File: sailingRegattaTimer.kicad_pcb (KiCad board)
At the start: 2 copper layers, 25 parts, among them J1-Red-1M1 Conn_01x02_Socket, J10-12v-In1 Conn_01x02_Socket, J2-Yel-2M1 Conn_01x02_Socket, J3-Grn-3M1 J3-Grn-3M, J4-Blu-5M1 J4-Blu-5M1, J5-5v-LED1 Conn_01x02_Socket, J6-Reset1 J6-Reset, J7-Ext-Buz1 Conn_01x02_Socket, J8-Pololu-VReg1 Conn_01x04_Socket, J9-Relay1 Conn_01x03_Socket

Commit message: incremental save updated schematic and pcb
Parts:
- moved R5 60.7 mm to (160.1, 64.0)
- moved J8-Pololu-VReg1 49.2 mm to (168.0, 48.7)
- moved J10-12v-In1 46.1 mm to (176.0, 51.8)
- moved J9-Relay1 37.3 mm to (171.0, 78.9)
- moved J3-Grn-3M1 32.9 mm to (210.5, 71.8)
- moved J4-Blu-5M1 32.8 mm to (210.5, 80.8)
- moved R2 32.1 mm to (202.5, 64.6)
- moved J2-Yel-2M1 32.0 mm to (210.5, 62.2)
- moved J1-Red-1M1 31.6 mm to (210.5, 52.8)
- moved R1 31.5 mm to (202.5, 55.3)
- moved R4 31.5 mm to (202.5, 83.3)
- moved R3 31.5 mm to (202.5, 74.0)
- moved SW4-Blu-5M1 30.2 mm to (191.5, 79.3)
- moved SW3-Grn-3M1 30.0 mm to (191.5, 70.0)
- moved J5-5v-LED1 29.9 mm to (163.5, 82.0)
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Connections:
- A1 pad 29: unconnected-(A1-GND-Pad29) -> GND
- A1 pad 5: unconnected-(A1-+5V-Pad5) -> +5V
- A1 pad 6: unconnected-(A1-GND-Pad6) -> GND
- A1 pad 7: unconnected-(A1-GND-Pad7) -> GND
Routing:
- net GND: track 0.00 -> 180.1 mm
- net +5V: track 0.00 -> 110.7 mm
- net Net-(A1-D4): track 0.00 -> 70.5 mm
- net Net-(A1-~{RESET}): track 0.00 -> 67.9 mm
- net Net-(A1-D2): track 0.00 -> 55.0 mm
- net Net-(A1-D7): track 0.00 -> 45.1 mm, vias 0 -> 1
- net Net-(A1-D8): track 0.00 -> 35.7 mm, vias 0 -> 1
- net Net-(A1-VIN): track 0.00 -> 34.8 mm
- net Net-(A1-D12): track 0.00 -> 29.0 mm
- net Net-(A1-D3): track 0.00 -> 27.3 mm
- net Net-(A1-D5): track 0.00 -> 22.9 mm
- net Net-(D1-LED1-K): track 0.00 -> 21.3 mm
- net Net-(J10-12v-In1-Pin_1): track 0.00 -> 8.21 mm
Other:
- board text added: "+"
- board text added: "GND"

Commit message: remove production files, update schematic and pcb
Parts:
- A1: footprint Module:Arduino_UNO_R3 -> rt-uno:rt-Arduino_UNO_R3
- R1, R2, R3, R4: value ~ -> R; footprint Resistor_THT:R_Axial_DIN0309_L9.0mm_D3.2mm_P2.54mm_Vertical -> Resistor_THT:R_Axial_DIN0204_L3.6mm_D1.6mm_P1.90mm_Vertical
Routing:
- net +5V: track 110.7 -> 152.8 mm, vias 0 -> 1
- net GND: track 180.1 -> 201.2 mm
- net Net-(A1-D12): track 29.0 -> 44.5 mm
- net Net-(A1-D2): track 55.0 -> 62.7 mm
- net Net-(A1-~{RESET}): track 67.9 -> 74.4 mm
- net Net-(A1-D8): track 35.7 -> 42.2 mm
- net Net-(A1-D7): track 45.1 -> 51.6 mm
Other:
- board outline added: 69.5 x 54.5 mm
- board text added: "10"
- board text added: "11"
- board text added: "12"
- board text added: "13"
- board text added: "2"
- board text added: "3"
- board text added: "3V"
- board text added: "4"
- board text added: "5"
- board text added: "5V"
- board text added: "6"
- board text added: "7"
- board text added: "8"
- board text added: "9"
- board text added: "A0"
- board text added: "A1"
- board text added: "A2"
- board text added: "A3"
- board text added: "A4"
- board text added: "A5"
- board text added: "AREF"
- board text added: "IOREF"
- board text added: "RESET"
- board text added: "RX0"
- board text added: "Regatta Timer v1.5.0"
- board text added: "SCL"
- board text added: "SDA"
- board text added: "TX1"
- board text added: "VIN"

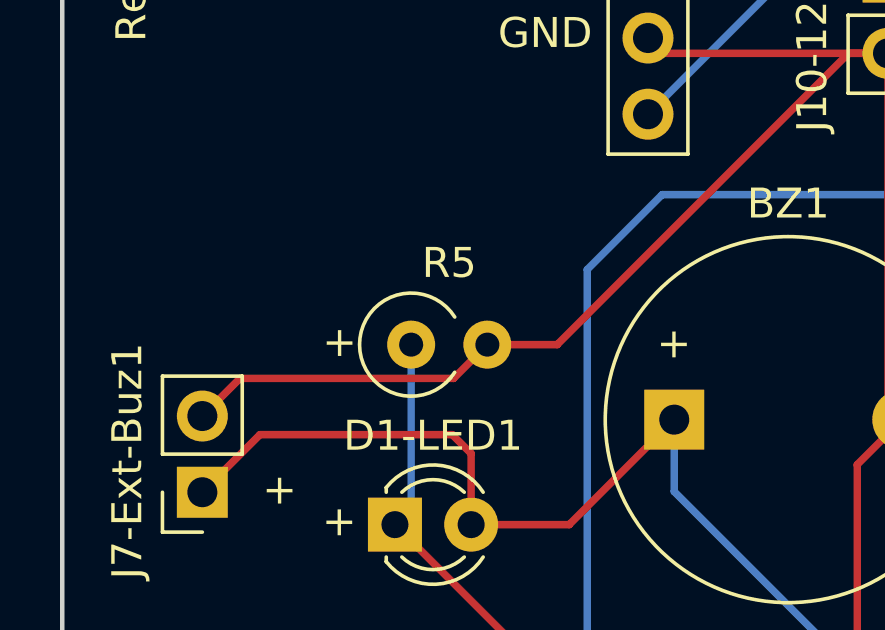
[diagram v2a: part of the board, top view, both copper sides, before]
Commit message: updated images and one resistor footprint so it matched the others
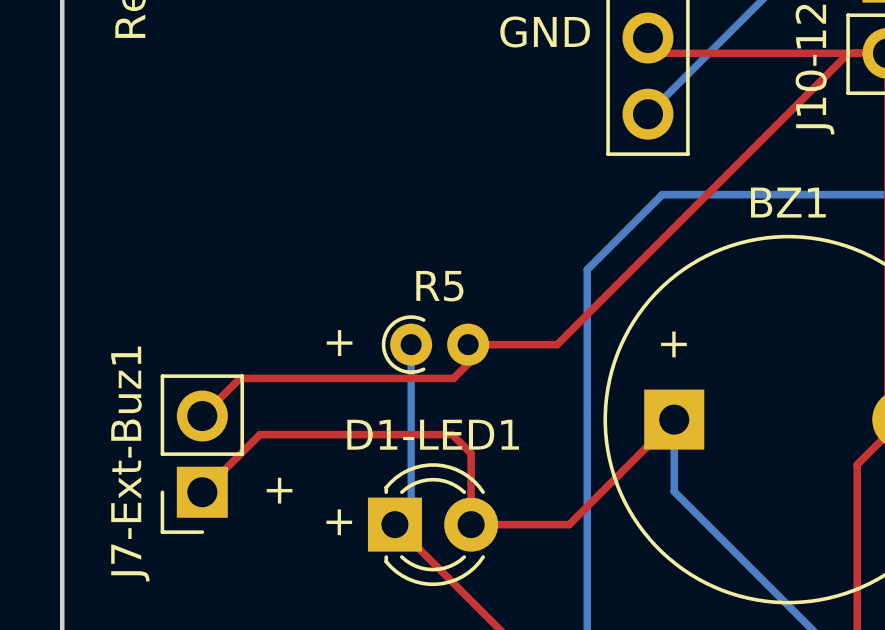
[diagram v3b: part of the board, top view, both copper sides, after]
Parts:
- R5: footprint Resistor_THT:R_Axial_DIN0309_L9.0mm_D3.2mm_P2.54mm_Vertical -> Resistor_THT:R_Axial_DIN0204_L3.6mm_D1.6mm_P1.90mm_Vertical
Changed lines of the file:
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@@
 		)
 	)
-	(footprint "Resistor_THT:R_Axial_DIN0309_L9.0mm_D3.2mm_P2.54mm_Vertical"
+	(footprint "Resistor_THT:R_Axial_DIN0204_L3.6mm_D1.6mm_P1.90mm_Vertical"
 		(layer "F.Cu")
 		(at 160.13 64)
-		(descr "Resistor, Axial_DIN0309 series, Axial, Vertical, pin pitch=2.54mm, 0.5W = 1/2W, length*diameter=9*3.2mm^2, http://cdn-reichelt.de/documents/datenblatt/B400/1_4W%23YAG.pdf")
-		(tags "Resistor Axial_DIN0309 series Axial Vertical pin pitch 2.54mm 0.5W = 1/2W length 9mm diameter 3.2mm")
+		(descr "Resistor, Axial_DIN0204 series, Axial, Vertical, pin pitch=1.9mm, 0.167W, length*diameter=3.6*1.6mm^2, http://cdn-reichelt.de/documents/datenblatt/B400/1_4W%23YAG.pdf")
+		(tags "Resistor Axial_DIN0204 series Axial Vertical pin pitch 1.9mm 0.167W length 3.6mm diameter 1.6mm")
 		(property "Reference" "R5"
-			(at 1.27 -2.72 0)
+			(at 0.95 -1.92 0)
 			(layer "F.SilkS")
 			(effects
@@
 		)
 		(property "Value" "~"
-			(at 1.27 2.72 0)
+			(at 0.95 1.92 0)
 			(layer "F.Fab")
-			(hide yes)
 			(effects
 				(font
@@
 		(attr through_hole)
 		(fp_arc
-			(start 1.453272 0.92)
-			(mid -1.72 0)
-			(end 1.453272 -0.92)
+			(start 0.417133 0.82)
+			(mid -0.92 0)
+			(end 0.417133 -0.82)
 			(stroke
 				(width 0.12)
@@
 		)
 		(fp_rect
-			(start -1.85 -1.85)
-			(end 3.59 1.85)
+			(start -1.05 -1.05)
+			(end 2.86 1.05)
 			(stroke
 				(width 0.05)
@@
 		(fp_line
 			(start 0 0)
-			(end 2.54 0)
+			(end 1.9 0)
 			(stroke
 				(width 0.1)
@@
 		(fp_circle
 			(center 0 0)
-			(end 1.6 0)
+			(end 0.8 0)
 			(stroke
 				(width 0.1)
@@
 		)
 		(fp_text user "${REFERENCE}"
-			(at 1.27 -2.72 0)
+			(at 0.95 -1.92 0)
 			(layer "F.Fab")
 			(effects
@@
 		(pad "1" thru_hole circle
 			(at 0 0)
-			(size 1.6 1.6)
-			(drill 0.8)
+			(size 1.4 1.4)
+			(drill 0.7)
 			(layers "*.Cu" "*.Mask")
 			(remove_unused_layers no)
@@
 		)
 		(pad "2" thru_hole circle
-			(at 2.54 0)
-			(size 1.6 1.6)
-			(drill 0.8)
+			(at 1.9 0)
+			(size 1.4 1.4)
+			(drill 0.7)
 			(layers "*.Cu" "*.Mask")
 			(remove_unused_layers no)
@@
 		)
 		(embedded_fonts no)
-		(model "${KICAD9_3DMODEL_DIR}/Resistor_THT.3dshapes/R_Axial_DIN0309_L9.0mm_D3.2mm_P2.54mm_Vertical.step"
+		(model "${KICAD9_3DMODEL_DIR}/Resistor_THT.3dshapes/R_Axial_DIN0204_L3.6mm_D1.6mm_P1.90mm_Vertical.step"
 			(offset
 				(xyz 0 0 0)
@@
 	)
 	(group ""
-		(members "97f0f6ec-2a6a-43d7-b072-60f9bf03ab03" "ec75d8e9-d7df-4479-9fa1-b60ede0a0817")
-	)
-	(group ""
 		(members "5d61b1c7-fe2e-49c8-87ca-db68f5c14beb" "9c1b1f79-0a0c-427c-aa09-aa0a06916a98")
 	)
@@
 	)
 	(group ""
+		(members "97f0f6ec-2a6a-43d7-b072-60f9bf03ab03" "ec75d8e9-d7df-4479-9fa1-b60ede0a0817")
+	)
+	(group ""

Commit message: incremental save
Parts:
- A1, BZ1, D1-LED1, J1-Red-1M1, J10-12v-In1, J2-Yel-2M1, J3-Grn-3M1, J4-Blu-5M1, J5-5v-LED1, J6-Reset1, J7-Ext-Buz1, J8-Pololu-VReg1, J9-Relay1, R2, R3, R4, R5, SW1-Red-1M1, SW2-Yel-2M1, SW3-Grn-3M1, SW4-Blu-5M1, SW5-Reset1, TM1637+5-GND1, TM1637-CLK-DIO1: moved to B.Cu
- R1: value R -> ${Reference}; moved to B.Cu
- moved SW5-Reset1 63.5 mm to (215.0, 90.5), turned to 180 degrees
- moved J7-Ext-Buz1 60.2 mm to (213.3, 68.9), turned to 0 degrees
- moved J1-Red-1M1 54.6 mm to (156.0, 52.8), turned to 180 degrees
- moved J2-Yel-2M1 54.6 mm to (156.0, 62.2), turned to 180 degrees
- moved J3-Grn-3M1 54.6 mm to (156.0, 71.8), turned to 180 degrees
- moved J4-Blu-5M1 54.6 mm to (156.0, 80.8), turned to 180 degrees
- moved D1-LED1 47.3 mm to (206.9, 70.0), turned to 180 degrees
- moved R5 46.2 mm to (206.4, 64.0), turned to 180 degrees
- moved J5-5v-LED1 39.4 mm to (203.0, 82.0), turned to 180 degrees
- moved J6-Reset1 39.4 mm to (203.0, 91.5), turned to 180 degrees
- moved R1 38.6 mm to (164.0, 55.3), turned to 180 degrees
- moved R2 38.6 mm to (164.0, 64.6), turned to 180 degrees
- moved R3 38.6 mm to (164.0, 74.0), turned to 180 degrees
- moved R4 38.6 mm to (164.0, 83.3), turned to 180 degrees
- moved J8-Pololu-VReg1 30.4 mm to (198.5, 48.7), turned to 180 degrees
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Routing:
- net Net-(A1-D5): track 22.9 -> 21.6 mm
- net Net-(A1-D3): track 27.3 -> 26.6 mm
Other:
- outline, holes or cut-outs redrawn
- board text added: "R1"
- board text added: "Regatta Timer v1.5.2"
- board text removed: "Regatta Timer v1.5.0"
